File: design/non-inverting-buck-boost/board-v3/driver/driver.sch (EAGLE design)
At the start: 0 parts

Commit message: finished driver schematic
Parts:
- added IC1: L7812, v-reg:78XXL
- added IC2: 78L05, v-reg:78LXX
- added IN: 22-23-2031, con-molex:22-23-2031
- added JUMPER, VBAT: 22-23-2021, con-molex:22-23-2021
- added OUT: 22-23-2041, con-molex:22-23-2041
- added R1, R2: (no value), resistor:R-US_0204/5
- added T1: BC547, transistor:BC547
- added U$1: B1209, felippe:B1209
- added U$2: ADUM3220, felippe:ADUM3220
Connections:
- new net GND: IC1.GND, IC2.GND, IN-3.S, OUT-4.S, T1.E, U$1.GND, U$2.GND1, VBAT-2.S
- new net N$1: IC1.OUT, IC2.IN, R2.2, U$1.VIN
- new net N$2: IC2.OUT, U$2.VDD1
- new net N$5: IC1.IN, VBAT-1.S
- new net N$6: IN-1.S, JUMPER-2.S, U$2.VIA
- new net N$7: IN-2.S, JUMPER-1.S, R1.1
- new net N$8: R1.2, T1.B
- new net VG1: OUT-1.S, U$1.VO, U$2.VDD2
- new net VG2: OUT-3.S, R2.1, T1.C
- new net VS1: OUT-2.S, U$1.0V, U$2.GND2

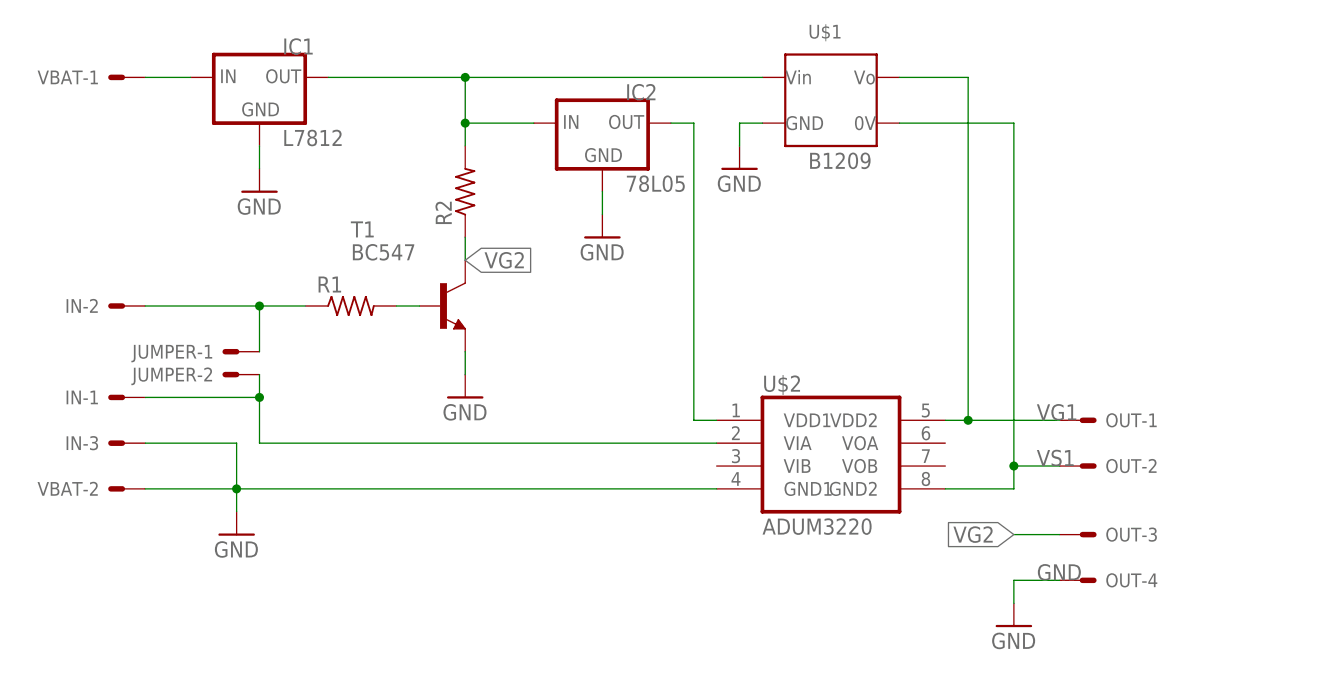
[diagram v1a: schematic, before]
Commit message: updated schematic - non inverting driver topology
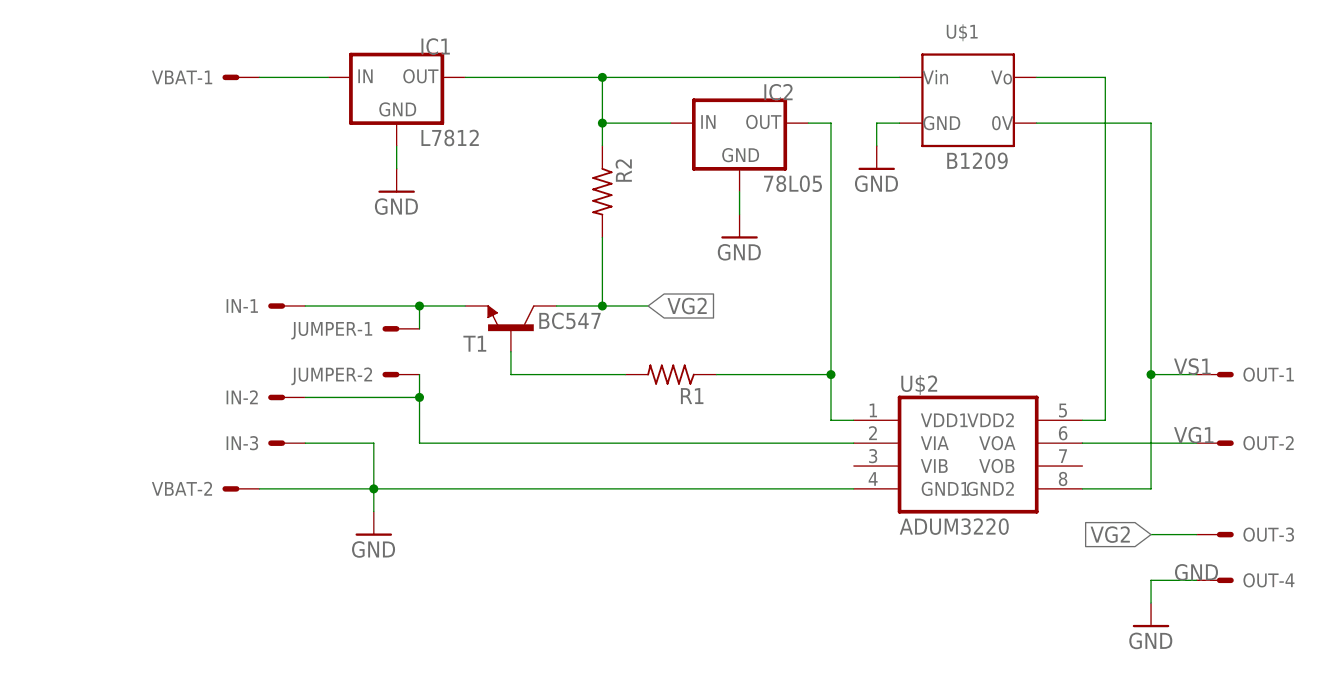
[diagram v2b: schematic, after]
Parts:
- R1, R2: device resistor:R-US_0204/5 -> resistor:R-US_0204/7
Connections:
- new net VDD2: U$1.VO, U$2.VDD2
- net GND: no longer T1.E
- net N$1: now also R2.1; no longer R2.2
- net N$2: now also R1.1
- net N$6: now also IN-2.S; no longer IN-1.S
- net N$7: now also IN-1.S, T1.E; no longer IN-2.S, R1.1
- net VG1: now also OUT-2.S, U$2.VOA; no longer OUT-1.S, U$1.VO, U$2.VDD2
- net VG2: now also R2.2; no longer R2.1
- net VS1: now also OUT-1.S; no longer OUT-2.S
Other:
- moved on the sheet: IC1, IC2, IN-1, IN-2, IN-3, JUMPER-1, JUMPER-2, OUT-1, OUT-2, OUT-3, OUT-4, R1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

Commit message: fixed ADuM3220 pins
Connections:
- net VG1: now also OUT-1.S; no longer OUT-2.S
- net VS1: now also OUT-2.S; no longer OUT-1.S
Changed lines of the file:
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@@
 <pinref part="U$1" gate="G$1" pin="0V"/>
 <wire x1="76.2" y1="68.58" x2="88.9" y2="68.58" width="0.1524" layer="91"/>
-<wire x1="88.9" y1="68.58" x2="88.9" y2="40.64" width="0.1524" layer="91"/>
+<wire x1="88.9" y1="68.58" x2="88.9" y2="33.02" width="0.1524" layer="91"/>
 <pinref part="U$2" gate="G$1" pin="GND2"/>
-<wire x1="88.9" y1="40.64" x2="88.9" y2="27.94" width="0.1524" layer="91"/>
+<wire x1="88.9" y1="33.02" x2="88.9" y2="27.94" width="0.1524" layer="91"/>
 <wire x1="88.9" y1="27.94" x2="81.28" y2="27.94" width="0.1524" layer="91"/>
-<pinref part="OUT" gate="-1" pin="S"/>
-<wire x1="93.98" y1="40.64" x2="88.9" y2="40.64" width="0.1524" layer="91"/>
-<junction x="88.9" y="40.64"/>
-<label x="91.44" y="40.64" size="1.778" layer="95"/>
+<pinref part="OUT" gate="-2" pin="S"/>
+<wire x1="93.98" y1="33.02" x2="88.9" y2="33.02" width="0.1524" layer="91"/>
+<junction x="88.9" y="33.02"/>
+<label x="91.44" y="33.02" size="1.778" layer="95"/>
 </segment>
 </net>
@@
 <net name="VG1" class="0">
 <segment>
-<pinref part="OUT" gate="-2" pin="S"/>
+<pinref part="OUT" gate="-1" pin="S"/>
+<wire x1="93.98" y1="40.64" x2="86.36" y2="40.64" width="0.1524" layer="91"/>
+<wire x1="86.36" y1="40.64" x2="86.36" y2="33.02" width="0.1524" layer="91"/>
 <pinref part="U$2" gate="G$1" pin="VOA"/>
-<wire x1="93.98" y1="33.02" x2="81.28" y2="33.02" width="0.1524" layer="91"/>
-<label x="91.44" y="33.02" size="1.778" layer="95"/>
+<wire x1="86.36" y1="33.02" x2="81.28" y2="33.02" width="0.1524" layer="91"/>
+<label x="91.44" y="40.64" size="1.778" layer="95"/>
 </segment>
 </net>
